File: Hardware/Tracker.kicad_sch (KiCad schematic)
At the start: 27 parts, among them J1 Battery, J11 SPI_Programming, J4 RX, J5 TX, J6 GND, J7 GND, J8 GND, J9 Haeder_LED, U1 L7805, U2 ATmega328P-P, Y1 16MHz

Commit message: Update of PCB
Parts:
- removed C5, C6: 22pF, Capacitor_THT:C_Disc_D4.7mm_W2.5mm_P5.00mm, symbol Device:C
- removed D6: LED_RBKG, Connector_PinHeader_1.27mm:PinHeader_1x04_P1.27mm_Vertical, symbol Device:LED_RBKG
- removed R21, R22, R23: 270, Resistor_THT:R_Axial_DIN0204_L3.6mm_D1.6mm_P5.08mm_Horizontal, symbol Device:R
- removed Y1: 16MHz, Crystal:Crystal_HC49-4H_Vertical, symbol Device:Crystal
- R1, R7: footprint Resistor_THT:R_Axial_DIN0204_L3.6mm_D1.6mm_P5.08mm_Horizontal -> Resistor_THT:R_Axial_DIN0207_L6.3mm_D2.5mm_P7.62mm_Horizontal
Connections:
- net GNSS/PPS: now also U2.14 (PB0); no longer U2.16 (PB2)
- net GNSS/RX: now also U2.15 (PB1); no longer U2.14 (PB0)
- net GNSS/TX: now also U2.16 (PB2); no longer U2.15 (PB1)
- net Motors/Pot_Measure: now reaches U2.26 (PC3)
- net Motors/EN_MOTOR renamed Motors/IN_B
- net Motors/IN1_MOTOR renamed Motors/ENABLE
- net Motors/IN2_MOTOR renamed Motors/IN_A
- net XTAL1 renamed Crystal/XTAl_1
- net XTAL2 renamed Crystal/XTAl_2
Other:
- added sheet Crystal (Xtal.kicad_sch)
- sheet GNSS ports: added GND; removed none
- sheet Motors ports: added ENABLE, GND, IN_A, IN_B, Pot_Measure; removed EN_MOTOR, IN1_MOTOR, IN2_MOTOR

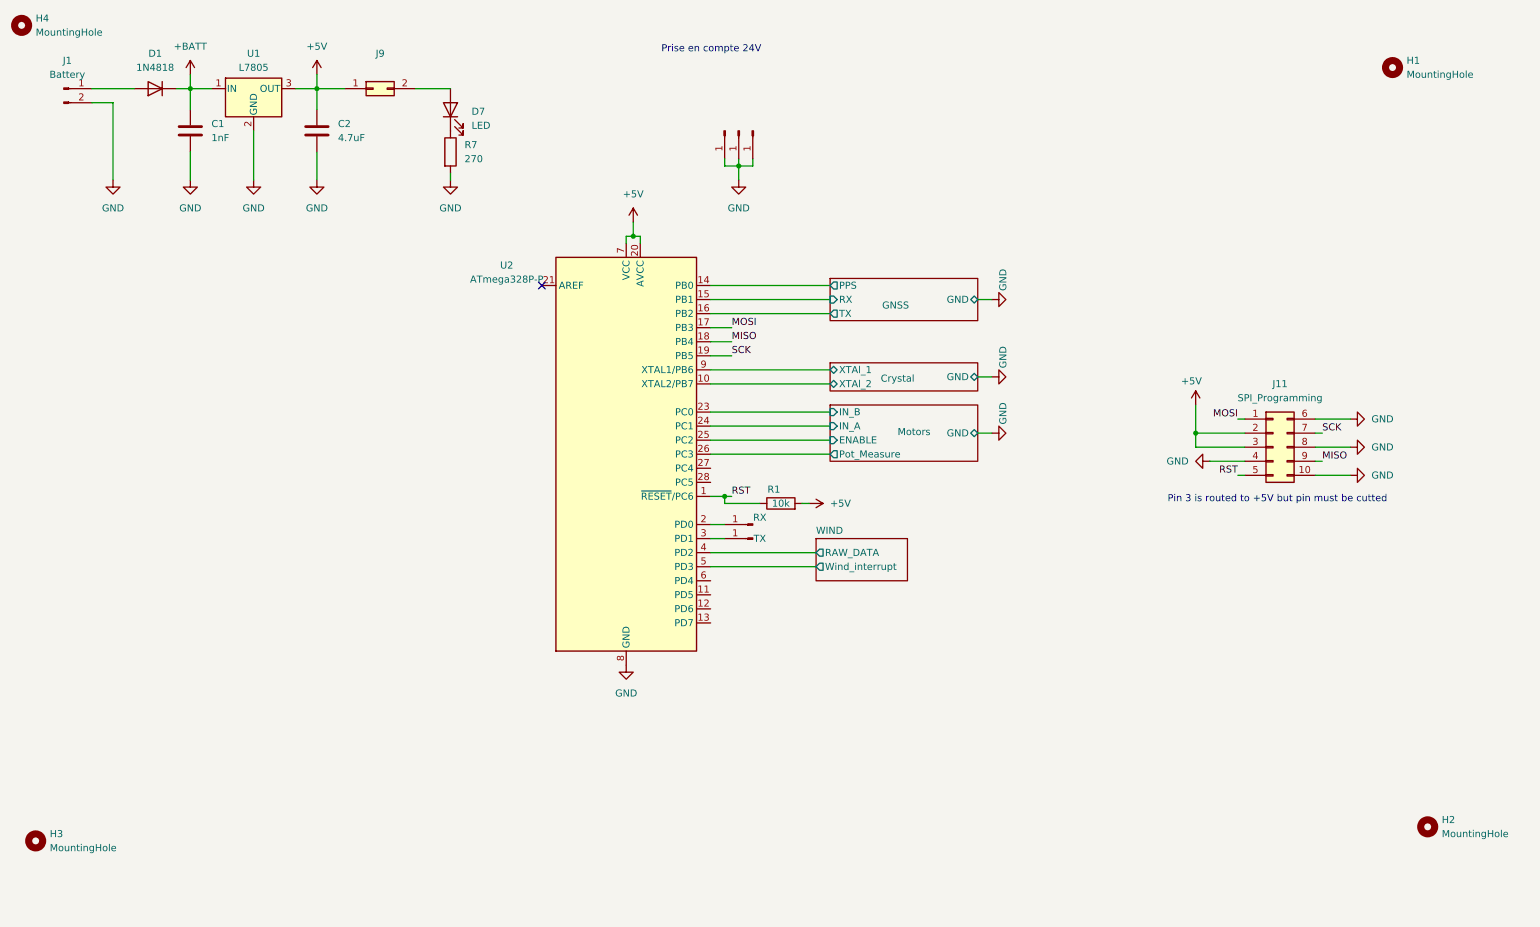
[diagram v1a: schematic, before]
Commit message: Update PCB of Motor controller - version sent on production (debug purpose)
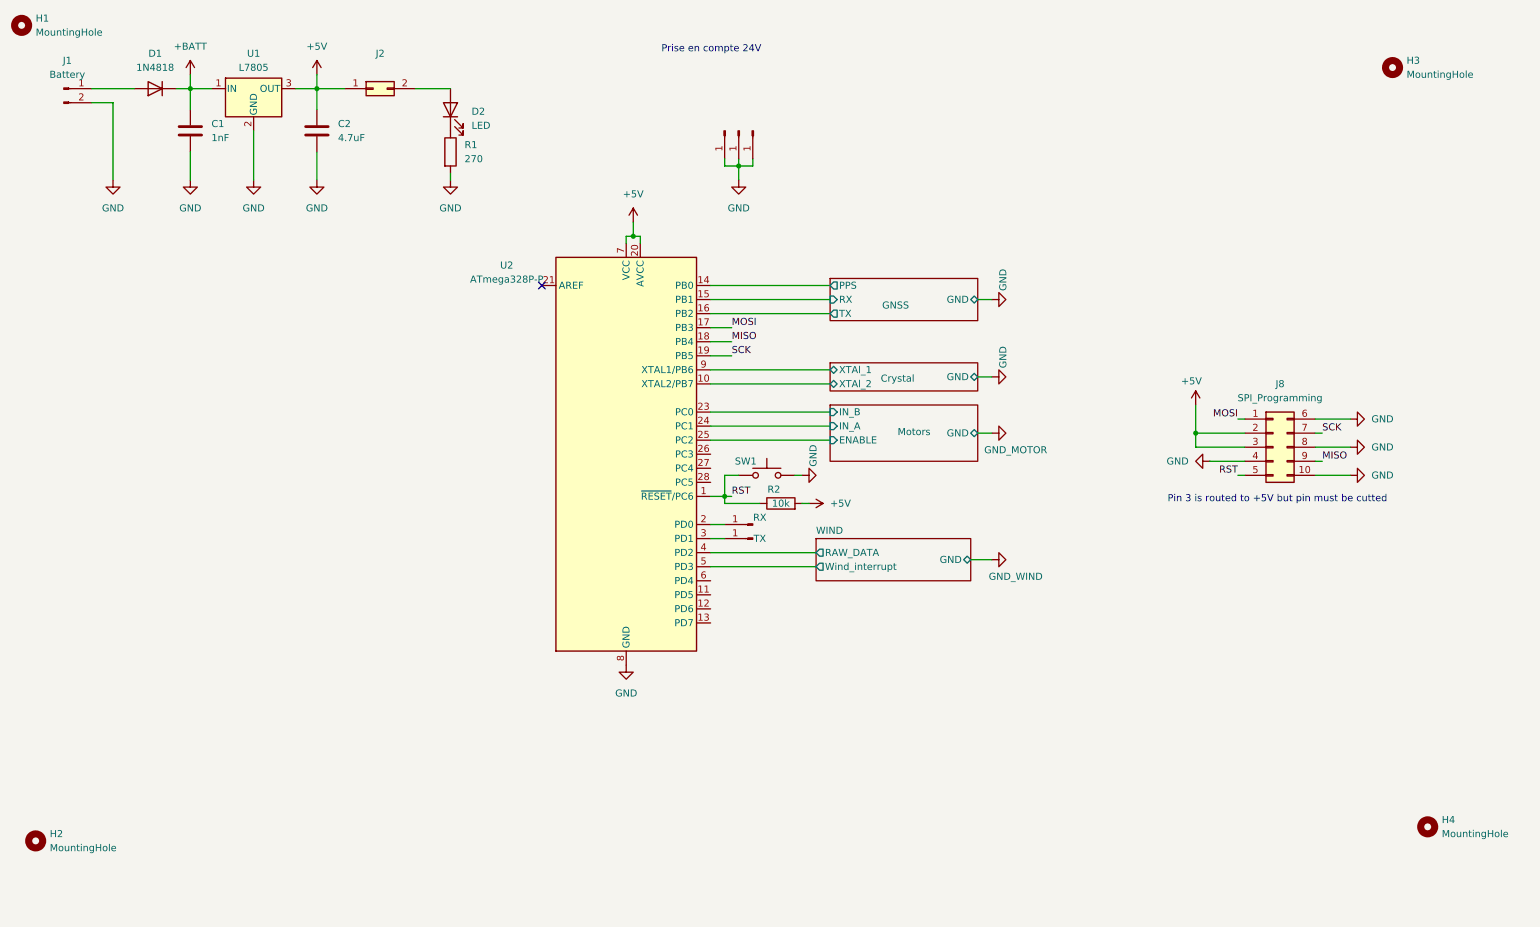
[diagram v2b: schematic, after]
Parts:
- added SW1: SW_Push, Button_Switch_THT:SW_PUSH_6mm, symbol Switch:SW_Push
- renumbered D7 to D2, H4 to H1, H3 to H2, H1 to H3, H2 to H4, J9 to J2, J6 to J3, J7 to J4, J8 to J5, J4 to J6, J5 to J7, J11 to J8, R7 to R1, R1 to R2
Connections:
- net GND: now also SW1.2
- net RST: now also SW1.1
- net Motors/Pot_Measure: no longer names the net of U2.26 (PC3)
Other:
- sheet Motors: file Motors.kicad_sch -> ../../../Electronique/Kicad/Motor_Control/Motor_Control.kicad_sch
- sheet Motors ports: added none; removed Pot_Measure
- sheet WIND ports: added GND; removed none

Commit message: Update of PCB
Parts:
- removed C1: 1nF, Capacitor_THT:C_Rect_L7.0mm_W2.0mm_P5.00mm, symbol Device:C
- removed C2: 4.7uF, Capacitor_THT:C_Radial_D5.0mm_H11.0mm_P2.00mm, symbol Device:C
- removed D1: 1N4818, Diode_THT:D_DO-41_SOD81_P7.62mm_Horizontal, symbol Device:D
- removed D2: LED, LED_THT:LED_D3.0mm, symbol Device:LED
- removed J1: Battery, TerminalBlock_Phoenix:TerminalBlock_Phoenix_MKDS-1,5-2-5.08_1x02_P5.08mm_Horizontal, symbol Connector:Conn_01x02_Pin
- removed J2: Haeder_LED, Connector_PinHeader_2.54mm:PinHeader_2x01_P2.54mm_Vertical, symbol Connector_Generic:Conn_02x01
- removed J3, J4, J5: GND, Connector_PinHeader_2.54mm:PinHeader_1x01_P2.54mm_Vertical, symbol Connector:Conn_01x01_Pin
- removed J6: RX, Connector_PinHeader_2.54mm:PinHeader_1x01_P2.54mm_Vertical, symbol Connector:Conn_01x01_Pin
- removed J7: TX, Connector_PinHeader_2.54mm:PinHeader_1x01_P2.54mm_Vertical, symbol Connector:Conn_01x01_Pin
- removed J8: SPI_Programming, Connector_PinHeader_2.54mm:PinHeader_2x05_P2.54mm_Vertical, symbol Connector_Generic:Conn_02x05_Top_Bottom
- removed R1: 270, Resistor_THT:R_Axial_DIN0207_L6.3mm_D2.5mm_P7.62mm_Horizontal, symbol Device:R
- removed R2: 10k, Resistor_THT:R_Axial_DIN0207_L6.3mm_D2.5mm_P7.62mm_Horizontal, symbol Device:R
- removed SW1: SW_Push, Button_Switch_THT:SW_PUSH_6mm, symbol Switch:SW_Push
- removed U1: L7805, Package_TO_SOT_THT:TO-220-3_Vertical, symbol Regulator_Linear:L7805
- removed U2: ATmega328P-P, Package_DIP:DIP-28_W7.62mm, symbol MCU_Microchip_ATmega:ATmega328P-P
- added R31: 1k, Resistor_THT:R_Axial_DIN0207_L6.3mm_D2.5mm_P7.62mm_Horizontal, symbol Device:R
- added R32: 2.2k, Resistor_THT:R_Axial_DIN0207_L6.3mm_D2.5mm_P7.62mm_Horizontal, symbol Device:R
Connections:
- new net TIMEPULSE: R32.2
- new net UserActions/Button: R31.2
- new net V_{A_{2}}: R31.1, R32.1
- no-connect marks 1 -> 7
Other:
- added sheet Anemometer (Modules/Anemometer.kicad_sch)
- added sheet MCU (Modules/MCU.kicad_sch)
- added sheet OLED (Modules/OLED.kicad_sch)
- added sheet Power_Supply (Modules/Power_supply.kicad_sch)
- added sheet Programming (Modules/Programming.kicad_sch)
- added sheet RTC (Modules/RTC.kicad_sch)
- added sheet Reset (Modules/Reset.kicad_sch)
- added sheet Stepper (Modules/Stepper.kicad_sch)
- added sheet UserActions (UserActions.kicad_sch)
- added sheet Wifi (Modules/Wifi.kicad_sch)
- sheet Crystal: file Xtal.kicad_sch -> Modules/Xtal.kicad_sch
- sheet GNSS: file GNSS.kicad_sch -> Modules/GNSS.kicad_sch
- sheet GNSS ports: added +3.3V_BACKUP, +3.3V_GNSS, GND_GNSS, TIMEPULSE, {UART}, ~{INTERNAL_ANTENNA}; removed GND, PPS, RX, TX
- sheet Motors ports: added +24V, Analog_position, M_ENABLE, M_IN_A, M_IN_B; removed ENABLE, IN_A, IN_B
- sheet WIND: file WIND.kicad_sch -> Modules/WIND.kicad_sch
- sheet WIND ports: added +5V; removed RAW_DATA
- note added: "TIMEPULSE == 0 && Button == Released : V_{A2} = 0V TIMEPULSE == 0 && Button == Pressed : V_{A2} = Vcc TIMEPULSE == 1 && Button == Released : V_{A2} = 5*({R31:value}/({R31:value})) TIMEPULSE == 1 && Button == Pressed : V_{A2} = 5*({R31:value}/({R31:value}))"
- note removed: "Pin 3 is routed to +5V but pin must be cutted"
- note removed: "Prise en compte 24V"
- title: SunTracker -> SunTracker - Hierarchical schematic
- moved on the sheet: H2
